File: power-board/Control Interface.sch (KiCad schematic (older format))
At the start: 3 parts, among them J2 CONN_02X05

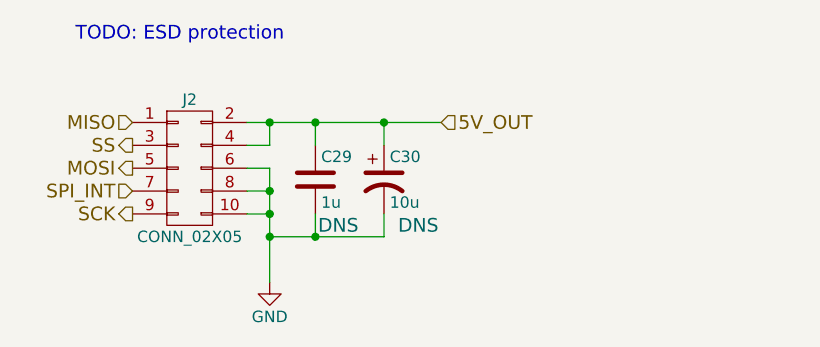
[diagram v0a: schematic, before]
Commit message: changed MCU to run at 3.3v
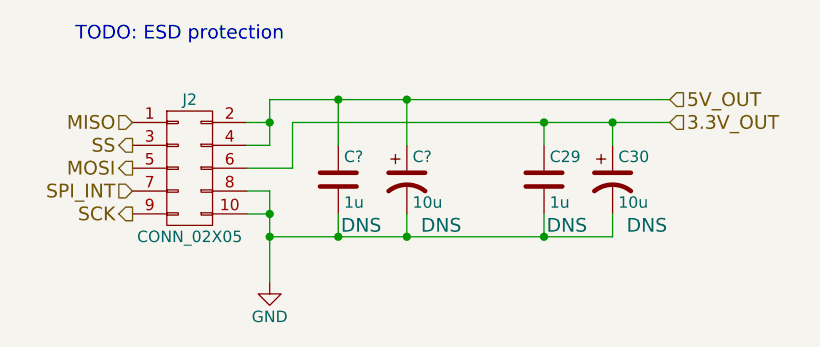
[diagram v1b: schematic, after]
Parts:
- added C?: 10u, symbol CP1
- added C?: 1u, symbol C
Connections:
- net 5V_OUT: now also C?.1, C?.1; no longer C29.1, C30.1
- net GND: now also C?.2, C?.2; no longer J2.6 (P6)
- new net 3.3V_OUT: C29.1, C30.1, J2.6 (P6)
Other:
- moved on the sheet: C29, C30
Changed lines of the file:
@@
 $Descr A4 11693 8268
 encoding utf-8
-Sheet 8 9
+Sheet 8 10
 Title ""
 Date ""
@@
 Text HLabel 3500 2850 0    60   Output ~ 0
 SS
-Text HLabel 4850 2750 2    60   Input ~ 0
+Text HLabel 5850 2650 2    60   Input ~ 0
 5V_OUT
 Text HLabel 3500 3150 0    60   Output ~ 0
@@
 $EndComp
 Wire Wire Line
-	4100 2950 4100 3450
-Wire Wire Line
-	4100 2950 4000 2950
-Wire Wire Line
 	4100 3050 4000 3050
-Connection ~ 4100 3050
 Wire Wire Line
 	4100 3150 4000 3150
 Connection ~ 4100 3150
 Wire Wire Line
-	4000 2750 4850 2750
+	4100 2850 4000 2850
 Wire Wire Line
-	4000 2850 4100 2850
-Wire Wire Line
-	4100 2850 4100 2750
+	4100 2650 4100 2850
 Connection ~ 4100 2750
 $Comp
 L CP1 C30
 U 1 1 593A43AA
-P 4600 3000
-F 0 "C30" H 4625 3100 50  0000 L CNN
-F 1 "10u" H 4625 2900 50  0000 L CNN
-F 2 "" H 4600 3000 50  0001 C CNN
-F 3 "" H 4600 3000 50  0001 C CNN
-F 4 "DNS" H 4750 2800 60  0000 C CNN "Note"
-F 5 "Samsung" H 4600 3000 60  0001 C CNN "MFG"
-F 6 "CL21A106KOQNNNG" H 4600 3000 60  0001 C CNN "MPN"
-	1    4600 3000
+P 5600 3000
+F 0 "C30" H 5625 3100 50  0000 L CNN
+F 1 "10u" H 5625 2900 50  0000 L CNN
+F 2 "" H 5600 3000 50  0001 C CNN
+F 3 "" H 5600 3000 50  0001 C CNN
+F 4 "DNS" H 5750 2800 60  0000 C CNN "Note"
+F 5 "Samsung" H 5600 3000 60  0001 C CNN "MFG"
+F 6 "CL21A106KOQNNNG" H 5600 3000 60  0001 C CNN "MPN"
+	1    5600 3000
 	1    0    0    -1
 $EndComp
@@
 L C C29
 U 1 1 593A43D3
-P 4300 3000
-F 0 "C29" H 4325 3100 50  0000 L CNN
-F 1 "1u" H 4325 2900 50  0000 L CNN
-F 2 "" H 4338 2850 50  0001 C CNN
-F 3 "" H 4300 3000 50  0001 C CNN
-F 4 "DNS" H 4400 2800 60  0000 C CNN "Note"
-F 5 "Samsung" H 4300 3000 60  0001 C CNN "MFG"
-F 6 "CL10B105KO8NNNC" H 4300 3000 60  0001 C CNN "MPN"
-	1    4300 3000
+P 5300 3000
+F 0 "C29" H 5325 3100 50  0000 L CNN
+F 1 "1u" H 5325 2900 50  0000 L CNN
+F 2 "" H 5338 2850 50  0001 C CNN
+F 3 "" H 5300 3000 50  0001 C CNN
+F 4 "DNS" H 5400 2800 60  0000 C CNN "Note"
+F 5 "Samsung" H 5300 3000 60  0001 C CNN "MFG"
+F 6 "CL10B105KO8NNNC" H 5300 3000 60  0001 C CNN "MPN"
+	1    5300 3000
 	1    0    0    -1
 $EndComp
 Wire Wire Line
-	4100 3250 4600 3250
+	4100 3250 5600 3250
 Wire Wire Line
-	4600 3250 4600 3150
+	5600 3250 5600 3150
 Connection ~ 4100 3250
 Wire Wire Line
-	4300 3150 4300 3250
-Connection ~ 4300 3250
+	5300 3150 5300 3250
+Connection ~ 5300 3250
 Wire Wire Line
-	4300 2850 4300 2750
-Connection ~ 4300 2750
+	5300 2850 5300 2750
+Connection ~ 5300 2750
 Wire Wire Line
-	4600 2850 4600 2750
-Connection ~ 4600 2750
+	5600 2850 5600 2750
+Connection ~ 5600 2750
 Text Notes 3250 2400 0    60   ~ 0
 TODO: ESD protection
+Text HLabel 5850 2750 2    60   Input ~ 0
+3.3V_OUT
+Wire Wire Line
+	4100 3050 4100 3450
+$Comp
+L CP1 C?
+U 1 1 593B8723
+P 4700 3000
+F 0 "C?" H 4725 3100 50  0000 L CNN
+F 1 "10u" H 4725 2900 50  0000 L CNN
+F 2 "" H 4700 3000 50  0001 C CNN
+F 3 "" H 4700 3000 50  0001 C CNN
+F 4 "DNS" H 4850 2800 60  0000 C CNN "Note"
+F 5 "Samsung" H 4700 3000 60  0001 C CNN "MFG"
+F 6 "CL21A106KOQNNNG" H 4700 3000 60  0001 C CNN "MPN"
+	1    4700 3000
+	1    0    0    -1
+$EndComp
+$Comp
+L C C?
+U 1 1 593B872C
+P 4400 3000
+F 0 "C?" H 4425 3100 50  0000 L CNN
+F 1 "1u" H 4425 2900 50  0000 L CNN
+F 2 "" H 4438 2850 50  0001 C CNN
+F 3 "" H 4400 3000 50  0001 C CNN
+F 4 "DNS" H 4500 2800 60  0000 C CNN "Note"
+F 5 "Samsung" H 4400 3000 60  0001 C CNN "MFG"
+F 6 "CL10B105KO8NNNC" H 4400 3000 60  0001 C CNN "MPN"
+	1    4400 3000
+	1    0    0    -1
+$EndComp
+Wire Wire Line
+	4000 2950 4200 2950
+Wire Wire Line
+	4100 2650 5850 2650
+Wire Wire Line
+	4100 2750 4000 2750
+Wire Wire Line
+	4200 2950 4200 2750
+Wire Wire Line
+	4200 2750 5850 2750
+Wire Wire Line
+	4700 3150 4700 3250
+Connection ~ 4700 3250
+Wire Wire Line
+	4400 3150 4400 3250
+Connection ~ 4400 3250
+Wire Wire Line
+	4400 2850 4400 2650
+Connection ~ 4400 2650
+Wire Wire Line
+	4700 2850 4700 2650
+Connection ~ 4700 2650
 $EndSCHEMATC

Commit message: switched to XMEGA A4U
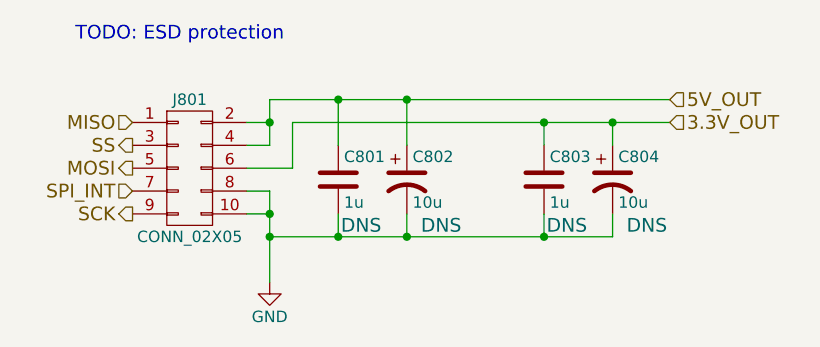
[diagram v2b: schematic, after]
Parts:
- gave numbers to parts that had none: 2
- renumbered C29 to C803, C30 to C804, J2 to J801
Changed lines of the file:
@@
 $Descr A4 11693 8268
 encoding utf-8
-Sheet 8 10
+Sheet 8 11
 Title ""
 Date ""
@@
 SPI_INT
 $Comp
-L CONN_02X05 J2
+L CONN_02X05 J801
 U 1 1 593A3868
 P 3750 2950
-F 0 "J2" H 3750 3250 50  0000 C CNN
+F 0 "J801" H 3750 3250 50  0000 C CNN
 F 1 "CONN_02X05" H 3750 2650 50  0000 C CNN
 F 2 "" H 3750 1750 50  0001 C CNN
@@
 $EndComp
 $Comp
-L GND #PWR36
+L GND #PWR044
 U 1 1 593A38A7
 P 4100 3450
-F 0 "#PWR36" H 4100 3200 50  0001 C CNN
+F 0 "#PWR044" H 4100 3200 50  0001 C CNN
 F 1 "GND" H 4100 3300 50  0000 C CNN
 F 2 "" H 4100 3450 50  0001 C CNN
@@
 Connection ~ 4100 2750
 $Comp
-L CP1 C30
+L CP1 C804
 U 1 1 593A43AA
 P 5600 3000
-F 0 "C30" H 5625 3100 50  0000 L CNN
+F 0 "C804" H 5625 3100 50  0000 L CNN
 F 1 "10u" H 5625 2900 50  0000 L CNN
 F 2 "" H 5600 3000 50  0001 C CNN
@@
 $EndComp
 $Comp
-L C C29
+L C C803
 U 1 1 593A43D3
 P 5300 3000
-F 0 "C29" H 5325 3100 50  0000 L CNN
+F 0 "C803" H 5325 3100 50  0000 L CNN
 F 1 "1u" H 5325 2900 50  0000 L CNN
 F 2 "" H 5338 2850 50  0001 C CNN
@@
 	4100 3050 4100 3450
 $Comp
-L CP1 C?
+L CP1 C802
 U 1 1 593B8723
 P 4700 3000
-F 0 "C?" H 4725 3100 50  0000 L CNN
+F 0 "C802" H 4725 3100 50  0000 L CNN
 F 1 "10u" H 4725 2900 50  0000 L CNN
 F 2 "" H 4700 3000 50  0001 C CNN
@@
 $EndComp
 $Comp
-L C C?
+L C C801
 U 1 1 593B872C
 P 4400 3000
-F 0 "C?" H 4425 3100 50  0000 L CNN
+F 0 "C801" H 4425 3100 50  0000 L CNN
 F 1 "1u" H 4425 2900 50  0000 L CNN
 F 2 "" H 4438 2850 50  0001 C CNN

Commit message: routed board
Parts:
- C801, C803: footprint (none) -> Capacitors_SMD:C_0603
- C802, C804: footprint (none) -> Capacitors_SMD:C_0805
- J801: footprint (none) -> Connectors:IDC_Header_Straight_10pins
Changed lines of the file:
@@
 $Descr A4 11693 8268
 encoding utf-8
-Sheet 8 11
+Sheet 7 12
 Title ""
 Date ""
@@
 F 0 "J801" H 3750 3250 50  0000 C CNN
 F 1 "CONN_02X05" H 3750 2650 50  0000 C CNN
-F 2 "" H 3750 1750 50  0001 C CNN
+F 2 "Connectors:IDC_Header_Straight_10pins" H 3750 1750 50  0001 C CNN
 F 3 "" H 3750 1750 50  0001 C CNN
 F 4 "3M Electronic Solutions Division" H 3750 2950 60  0001 C CNN "MFG"
@@
 $EndComp
 $Comp
-L GND #PWR044
+L GND #PWR030
 U 1 1 593A38A7
 P 4100 3450
-F 0 "#PWR044" H 4100 3200 50  0001 C CNN
+F 0 "#PWR030" H 4100 3200 50  0001 C CNN
 F 1 "GND" H 4100 3300 50  0000 C CNN
 F 2 "" H 4100 3450 50  0001 C CNN
@@
 F 0 "C804" H 5625 3100 50  0000 L CNN
 F 1 "10u" H 5625 2900 50  0000 L CNN
-F 2 "" H 5600 3000 50  0001 C CNN
+F 2 "Capacitors_SMD:C_0805" H 5600 3000 50  0001 C CNN
 F 3 "" H 5600 3000 50  0001 C CNN
 F 4 "DNS" H 5750 2800 60  0000 C CNN "Note"
@@
 F 0 "C803" H 5325 3100 50  0000 L CNN
 F 1 "1u" H 5325 2900 50  0000 L CNN
-F 2 "" H 5338 2850 50  0001 C CNN
+F 2 "Capacitors_SMD:C_0603" H 5338 2850 50  0001 C CNN
 F 3 "" H 5300 3000 50  0001 C CNN
 F 4 "DNS" H 5400 2800 60  0000 C CNN "Note"
@@
 F 0 "C802" H 4725 3100 50  0000 L CNN
 F 1 "10u" H 4725 2900 50  0000 L CNN
-F 2 "" H 4700 3000 50  0001 C CNN
+F 2 "Capacitors_SMD:C_0805" H 4700 3000 50  0001 C CNN
 F 3 "" H 4700 3000 50  0001 C CNN
 F 4 "DNS" H 4850 2800 60  0000 C CNN "Note"
@@
 F 0 "C801" H 4425 3100 50  0000 L CNN
 F 1 "1u" H 4425 2900 50  0000 L CNN
-F 2 "" H 4438 2850 50  0001 C CNN
+F 2 "Capacitors_SMD:C_0603" H 4438 2850 50  0001 C CNN
 F 3 "" H 4400 3000 50  0001 C CNN
 F 4 "DNS" H 4500 2800 60  0000 C CNN "Note"
